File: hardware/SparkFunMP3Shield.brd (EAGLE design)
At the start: 53.3 x 59.7 mm, 62 parts, among them J1 ISP/SPI, Q1 12.288MHz, U1 3.3V, U2 ARDUINO_R3_SHIELD, U3 VS1053, U4 1.8V, U6 USD-SOCKET, U7 74HC4050 LVL CONVERTER

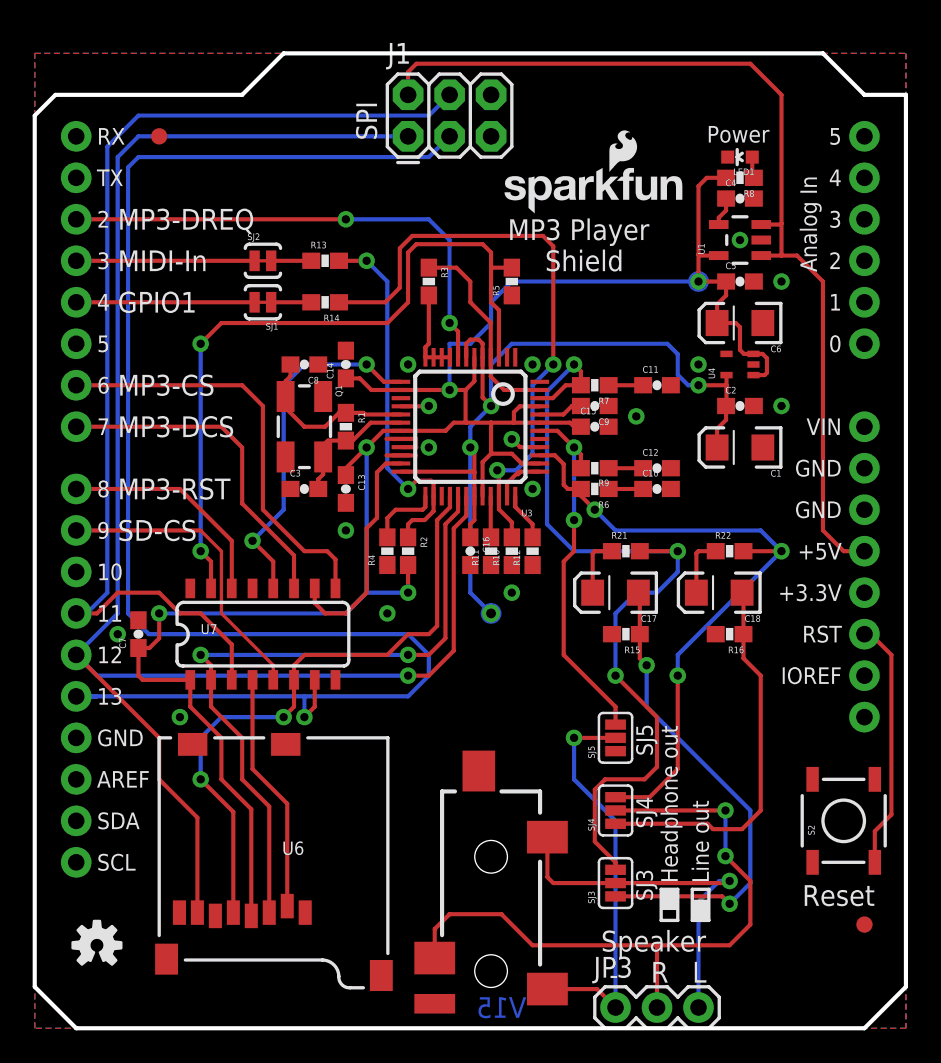
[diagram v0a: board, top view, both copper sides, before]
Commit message: Use traces to close jumpers
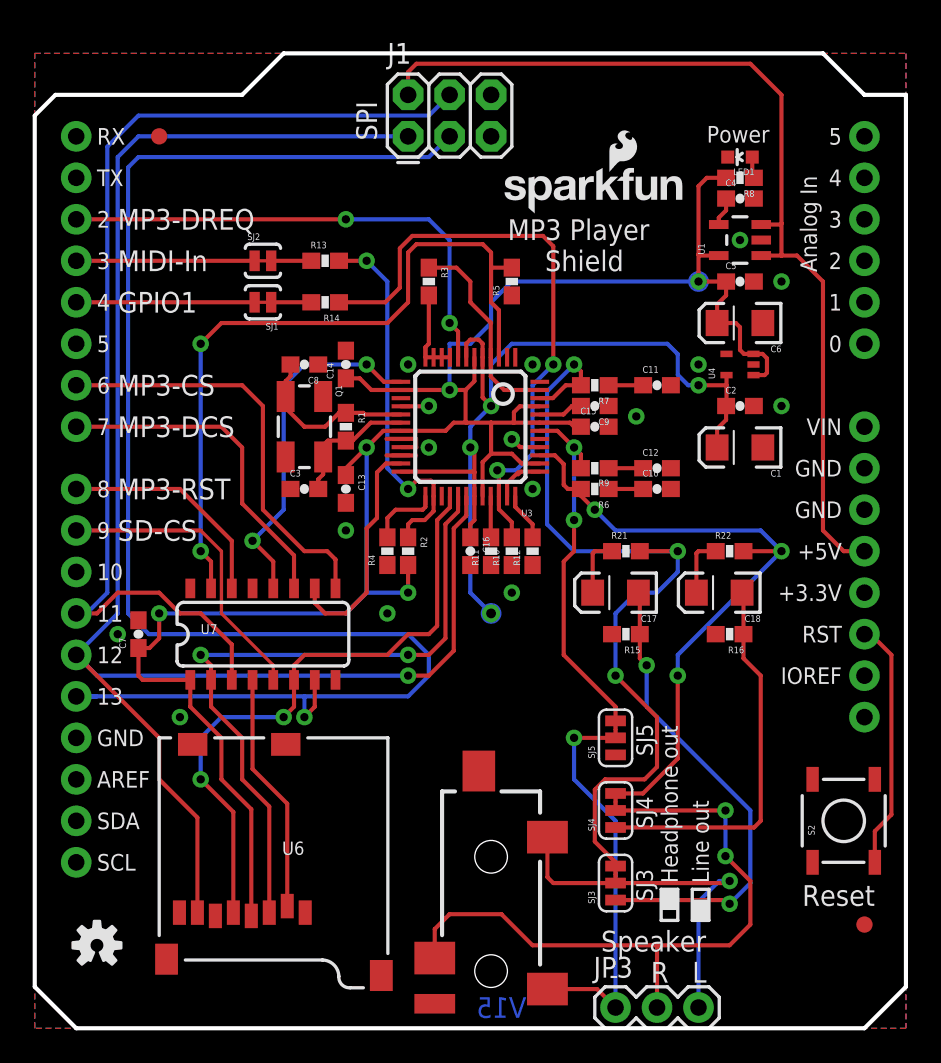
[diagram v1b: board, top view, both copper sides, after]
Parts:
- SJ3, SJ4, SJ5: device SparkFun-Passives:PAD-JUMPER-3-2OF3_NC_BY_PASTE_YES_SILK_FULL_BOX -> SparkFun-Jumpers:SMT-JUMPER_3_1-NC_TRACE_SILK
